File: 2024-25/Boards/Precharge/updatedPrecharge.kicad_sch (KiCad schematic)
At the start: 14 parts, among them J1 Conn_01x06, Q1 VN3205N3-G, Q2 VP3203N3-G, Q4 VP3203N3-G, U1 LM358DR2G

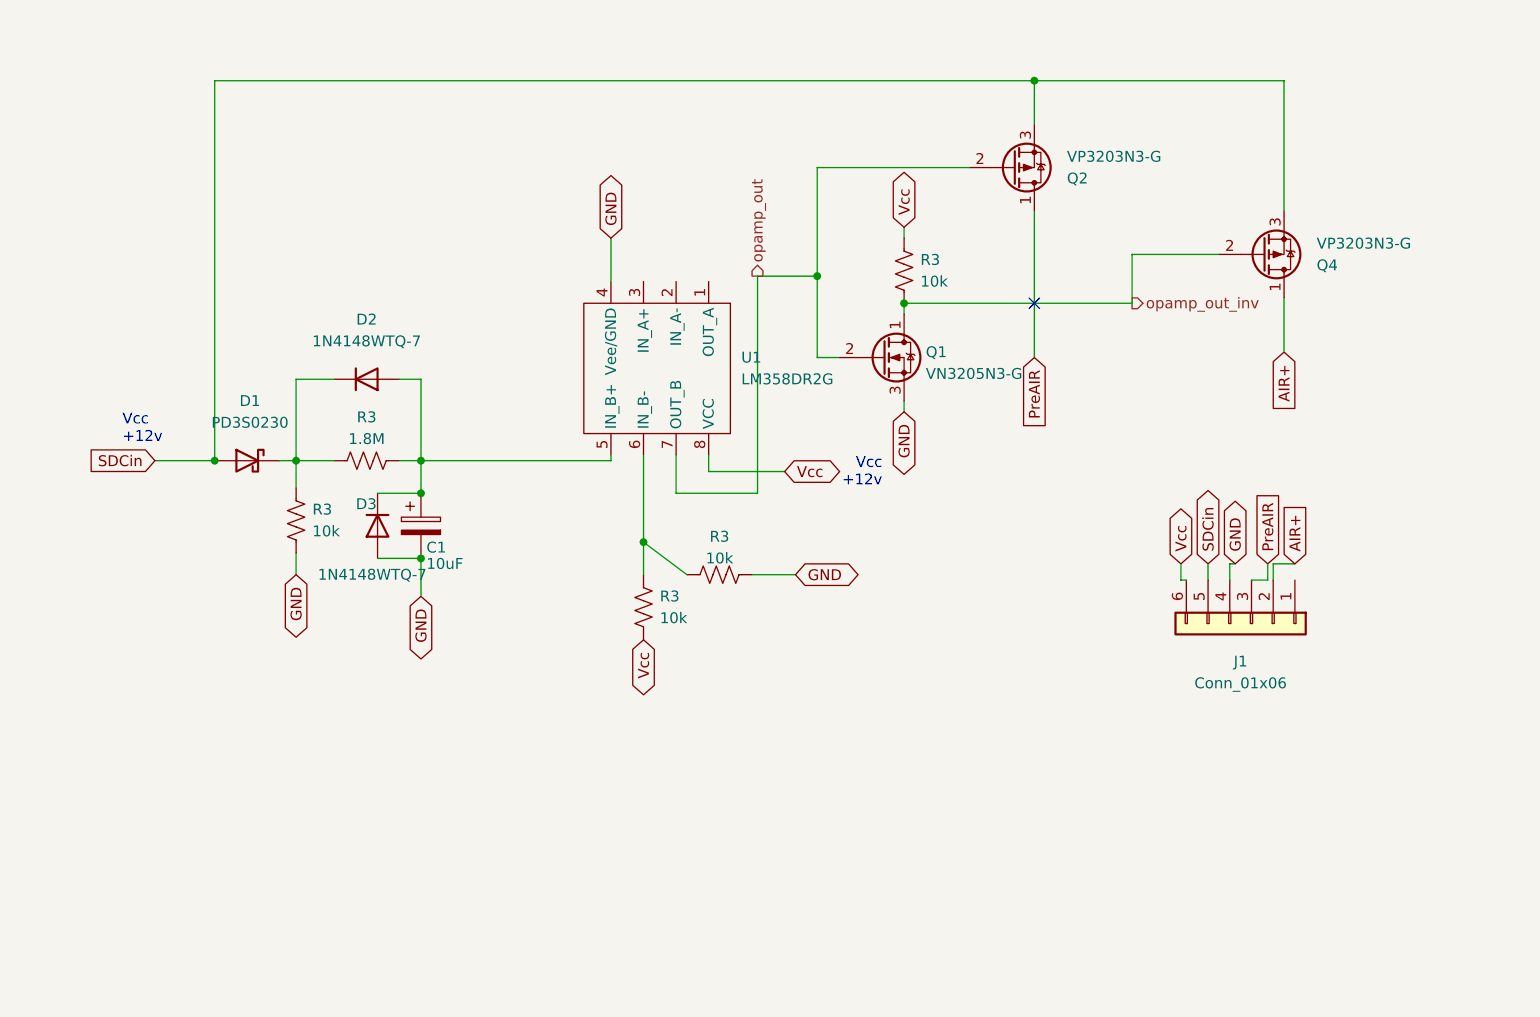
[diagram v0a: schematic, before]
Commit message: accum and HV box schm
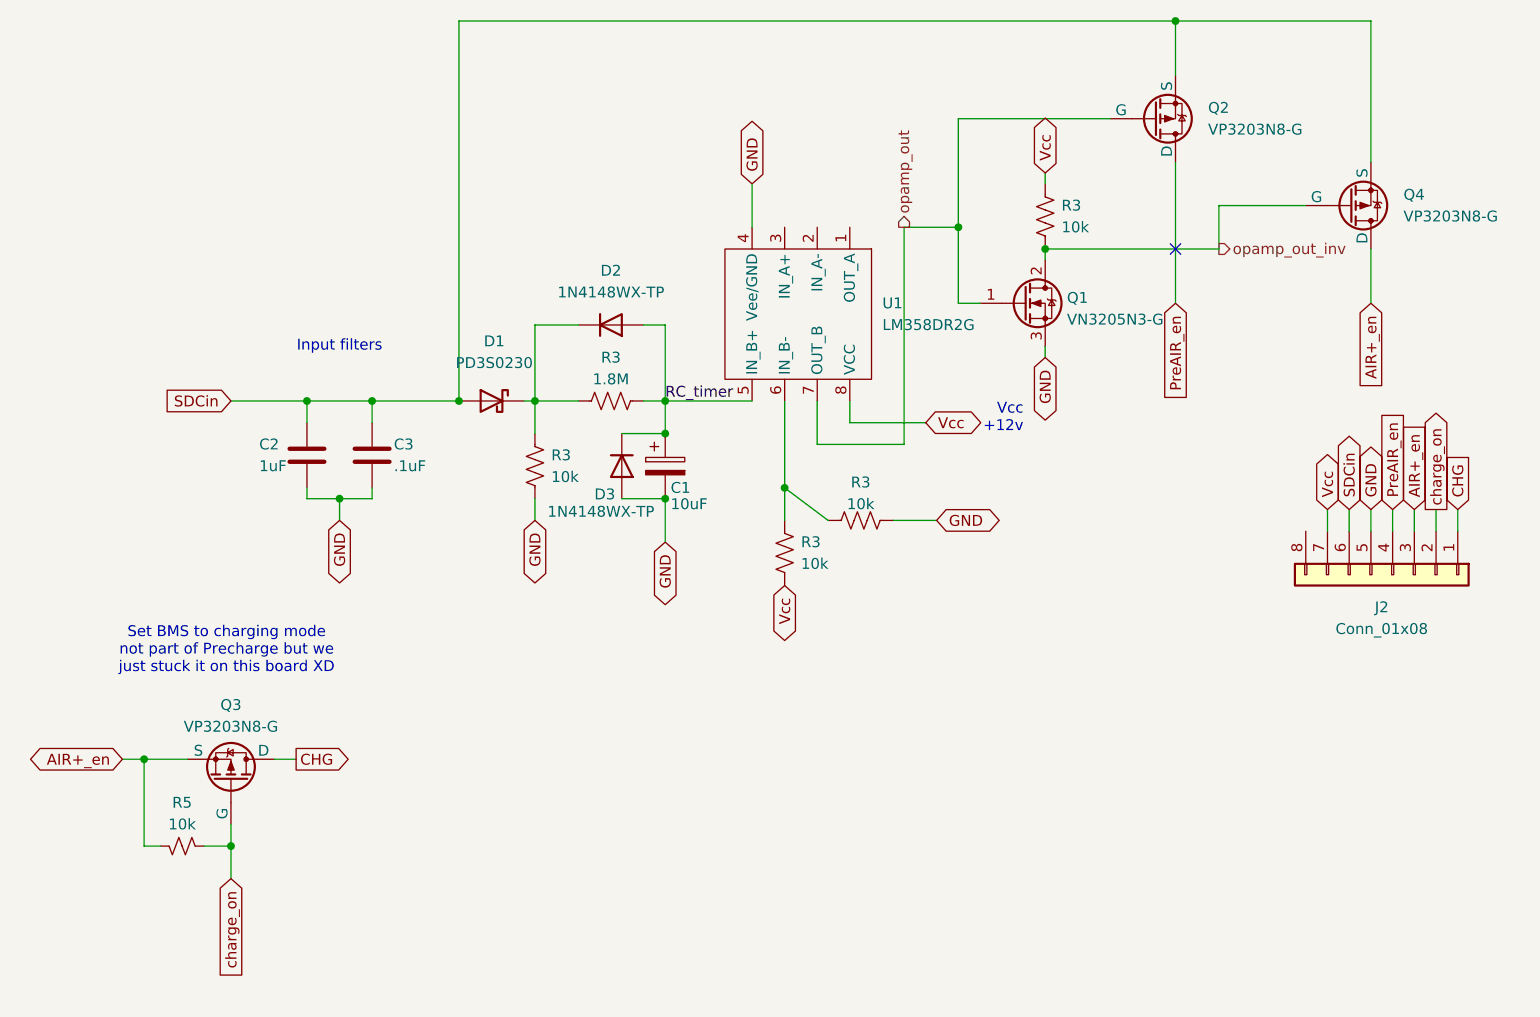
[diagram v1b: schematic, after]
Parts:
- removed J1: Conn_01x06, Connector_Molex:Molex_Micro-Fit_3.0_43045-0612_2x03_P3.00mm_Vertical, symbol Connector_Generic:Conn_01x06
- removed Q2, Q4: VP3203N3-G, Package_TO_SOT_THT:TO-92_Inline, symbol Transistor_FET:BS250
- added C2: 1uF, symbol Device:C
- added C3: .1uF, symbol Device:C
- added J2: Conn_01x08, Connector_Molex:Molex_Micro-Fit_3.0_43045-0812_2x04_P3.00mm_Vertical, symbol Connector_Generic:Conn_01x08
- added Q2, Q3, Q4: VP3203N8-G, VP3203N8-G:TO-243AA_MCH, symbol Simulation_SPICE:PMOS
- added R5: 10k, Resistor_SMD:R_0805_2012Metric_Pad1.20x1.40mm_HandSolder, symbol Device:R_Small_US
- C1: footprint Capacitor_THT:CP_Radial_D4.0mm_P2.00mm -> Capacitor_SMD:C_1206_3216Metric_Pad1.33x1.80mm_HandSolder
- D2, D3: value 1N4148WTQ-7 -> 1N4148WX-TP; footprint Diode_SMD:D_SOD-523 -> Diode_SMD:D_SOD-323
- Q1: footprint Package_TO_SOT_THT:TO-92_Inline -> VN3205N8-G:TO-243AA_MCH
- R3: footprint Resistor_THT:R_Axial_DIN0207_L6.3mm_D2.5mm_P7.62mm_Horizontal -> Resistor_SMD:R_0805_2012Metric_Pad1.20x1.40mm_HandSolder
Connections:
- net GND: now also C2.2, C3.2, J2.5 (Pin_5)
- net SDCin: now also C2.1, C3.1, J2.6 (Pin_6), Q2.3 (S), Q4.3 (S)
- net Vcc: now also J2.7 (Pin_7)
- net opamp_out: now also Q1.1 (G), Q2.1 (G); no longer Q1.2 (G)
- net opamp_out_inv: now also Q1.2 (D), Q4.1 (G); no longer Q1.1 (D)
- net RC_timer: now reaches C1.1, D2.2 (A), D3.1 (K), R3.1, U1.5 (IN_B+)
- new net AIR+_en: J2.3 (Pin_3), Q3.3 (S), Q4.2 (D), R5.1
- new net CHG: J2.1 (Pin_1), Q3.2 (D)
- new net PreAIR_en: J2.4 (Pin_4), Q2.2 (D)
- new net charge_on: J2.2 (Pin_2), Q3.1 (G), R5.2
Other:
- note added: "Input filters"
- note added: "Set BMS to charging mode not part of Precharge but we just stuck it on this board XD"
- moved on the sheet: C1, D1, D2, Q1, R3, U1

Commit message: checkbox schm
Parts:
- added H1, H2, H3, H4: MountingHole, MountingHole:MountingHole_4.3mm_M4, symbol Mechanical:MountingHole
- C2: footprint (none) -> Capacitor_SMD:C_0805_2012Metric_Pad1.18x1.45mm_HandSolder
- C3: footprint (none) -> Capacitor_SMD:C_0603_1608Metric_Pad1.08x0.95mm_HandSolder

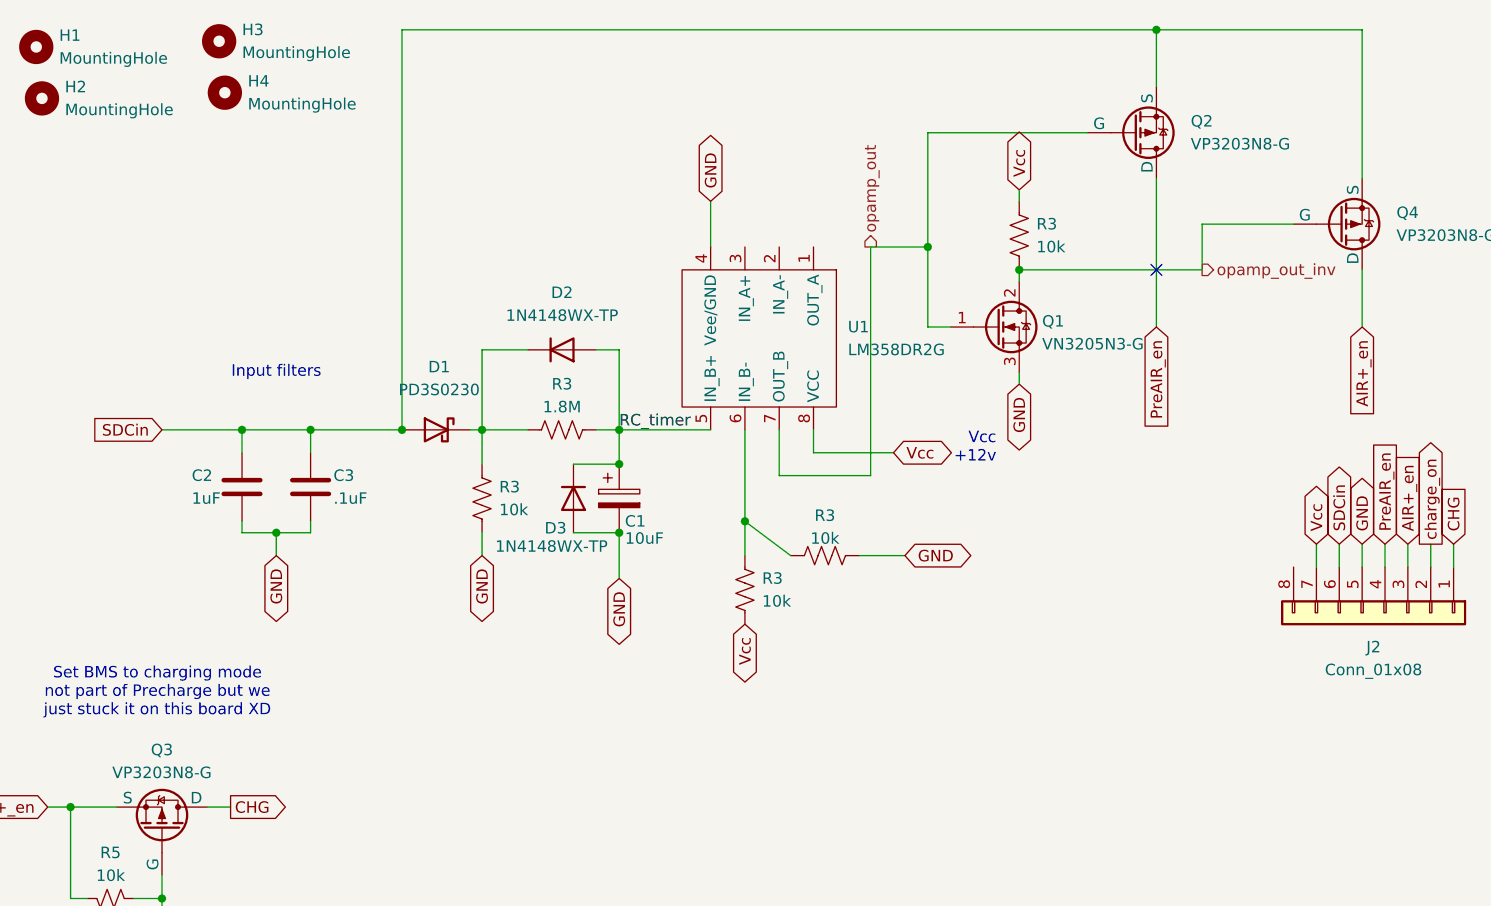
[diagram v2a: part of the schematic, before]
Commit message: fixed precharge layout
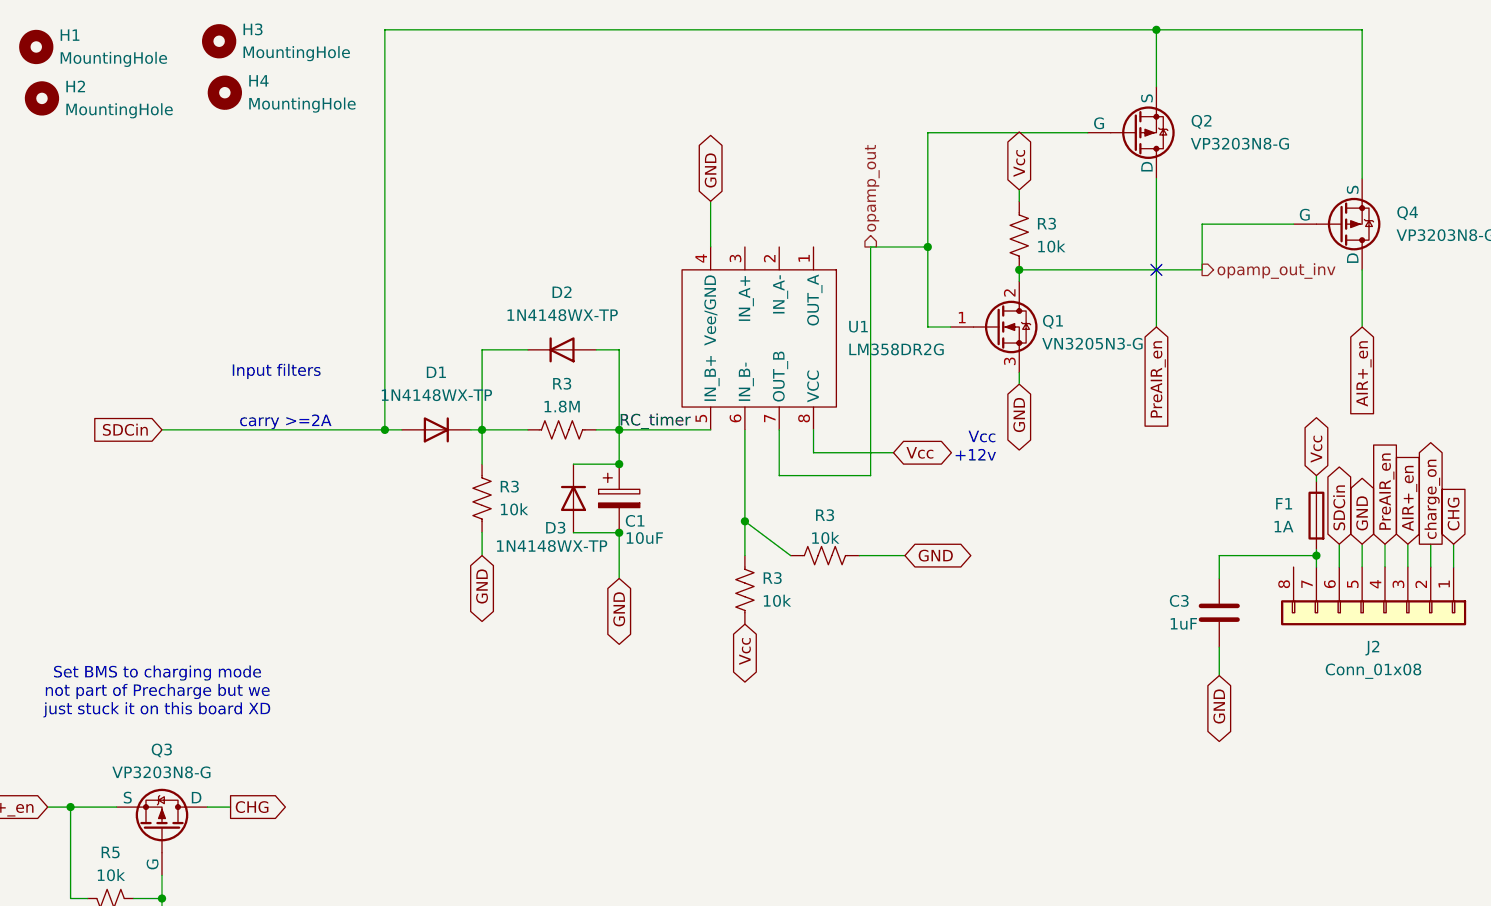
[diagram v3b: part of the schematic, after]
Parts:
- removed C2: 1uF, Capacitor_SMD:C_0805_2012Metric_Pad1.18x1.45mm_HandSolder, symbol Device:C
- removed D1: PD3S0230, Diode_SMD:D_SOD-110, symbol Device:D_Schottky
- added D1: 1N4148WX-TP, Diode_SMD:D_SOD-323, symbol Diode:BAV302
- added F1: 1A, Fuse:Fuse_Littelfuse_395Series, symbol Device:Fuse
- C3: value .1uF -> 1uF; footprint Capacitor_SMD:C_0603_1608Metric_Pad1.08x0.95mm_HandSolder -> Capacitor_SMD:C_0805_2012Metric_Pad1.18x1.45mm_HandSolder
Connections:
- net SDCin: now also D1.2 (A); no longer C3.1
- net Vcc: now also F1.1; no longer J2.7 (Pin_7)
- net at D2.1 (K), R3.2, R3.2: now also D1.1 (K)
- new net: C3.1, F1.2, J2.7 (Pin_7)
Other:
- note added: "carry >=2A"

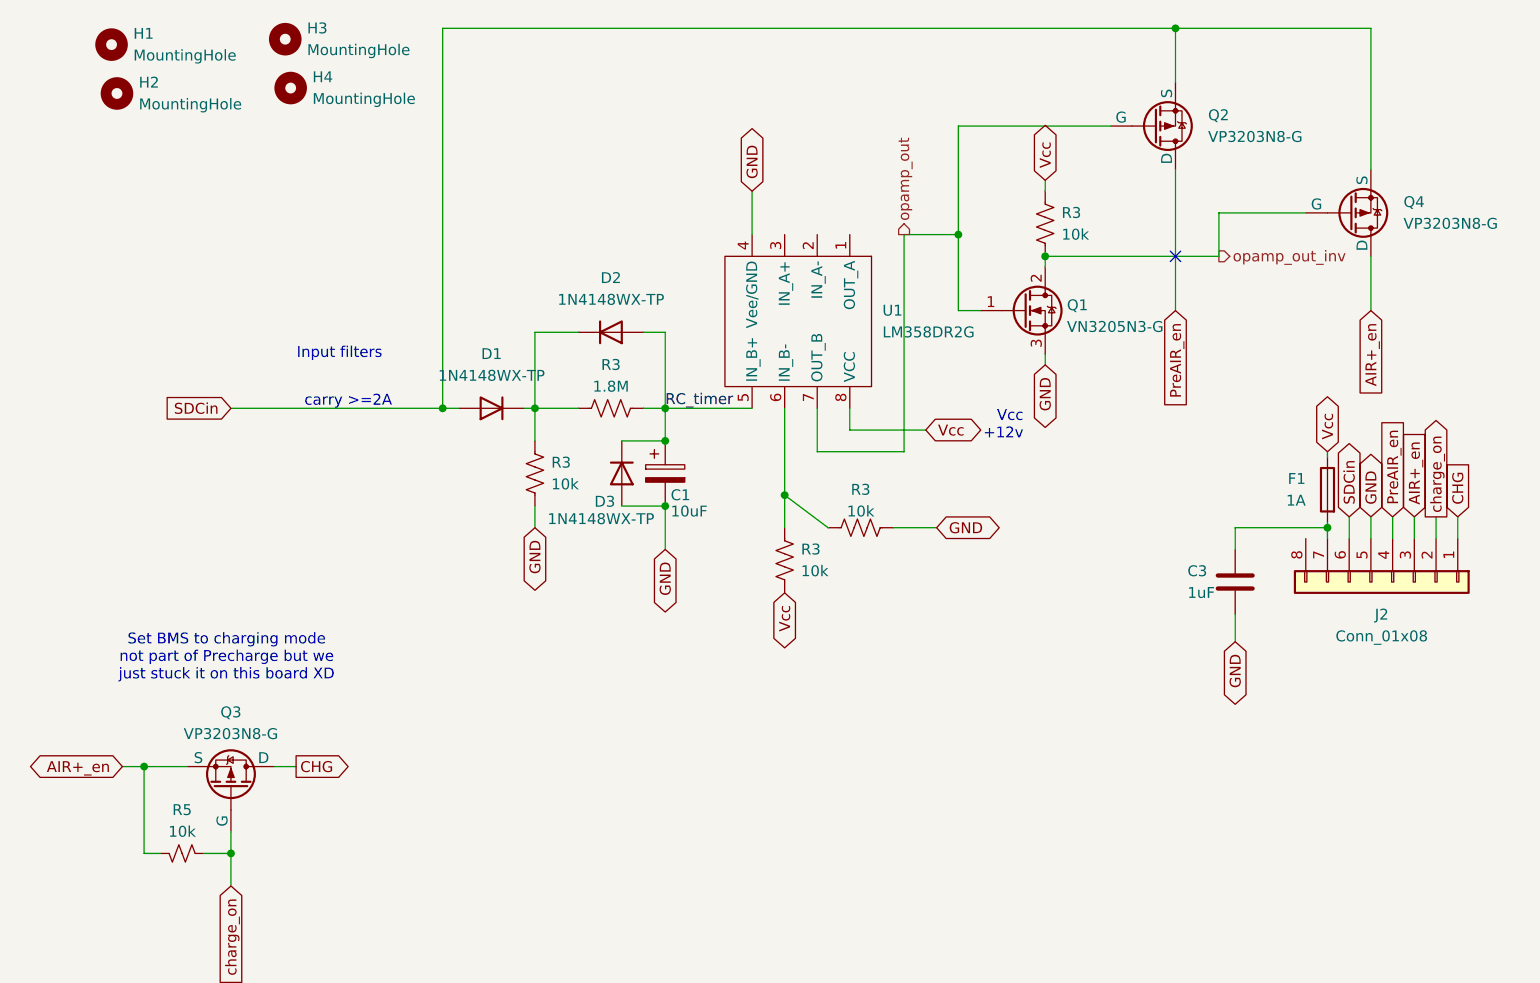
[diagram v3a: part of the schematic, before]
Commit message: made precharge orderable on jlcpcb
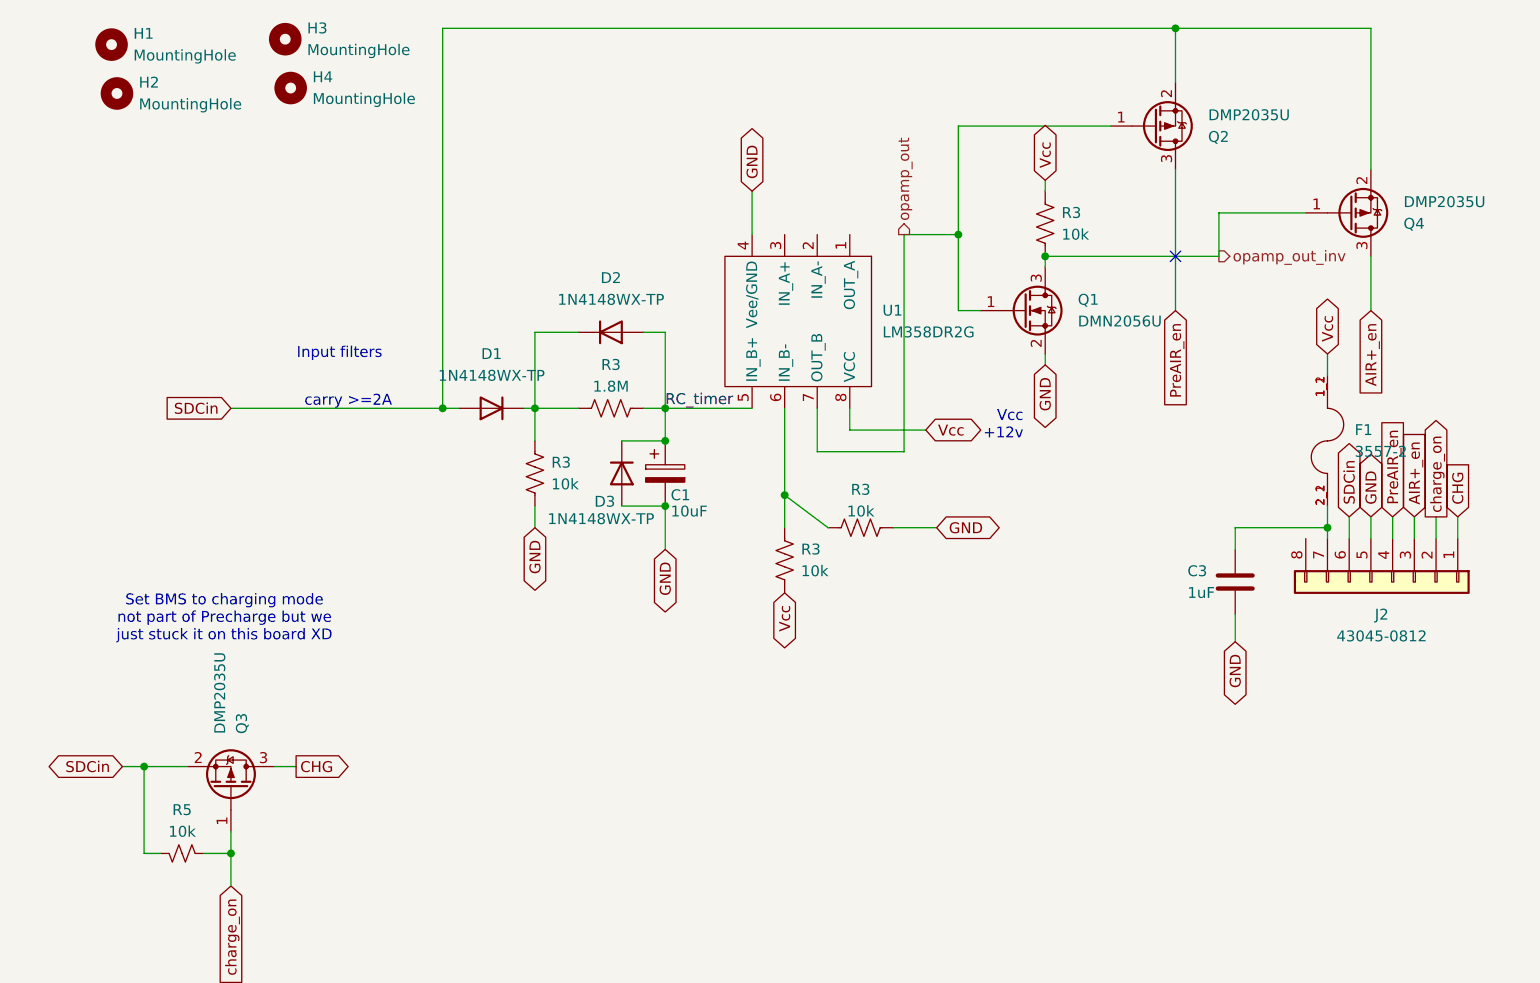
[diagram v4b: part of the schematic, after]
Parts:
- removed F1: 1A, Fuse:Fuse_Littelfuse_395Series, symbol Device:Fuse
- removed Q1: VN3205N3-G, VN3205N8-G:TO-243AA_MCH, symbol Transistor_FET:BS170
- removed Q2, Q3, Q4: VP3203N8-G, VP3203N8-G:TO-243AA_MCH, symbol Simulation_SPICE:PMOS
- added F1: 3557-2, Fuseholder:fuse, symbol 3557-2:3557-2
- added Q1: DMN2056U, Package_TO_SOT_SMD:SOT-23, symbol Transistor_FET:DMN2056U
- added Q2, Q3, Q4: DMP2035U, Package_TO_SOT_SMD:SOT-23, symbol Transistor_FET:AO3401A
- J2: value Conn_01x08 -> 43045-0812
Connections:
- net AIR+_en: now also Q4.3 (D); no longer R5.1
- net CHG: now also Q3.3 (D)
- net GND: now also Q1.2 (S)
- net PreAIR_en: now also Q2.3 (D)
- net SDCin: now also R5.1, Q2.2 (S), Q3.2 (S), Q4.2 (S)
- net Vcc: now also F1.1_1, F1.1_2
- net charge_on: now also Q3.1 (G)
- net opamp_out: now also Q1.1 (G), Q2.1 (G)
- net opamp_out_inv: now also Q1.3 (D), Q4.1 (G)
- net at C3.1, J2.7 (Pin_7): now also F1.2_1, F1.2_2
